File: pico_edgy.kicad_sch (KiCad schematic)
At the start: 18 parts, among them J2 001, J3 002, J4 007, J5 100, J6 100, J7 USB_C_Receptacle_USB2.0_16P, U4 USBLC6-2SC6, U5 AMS1117-3.3

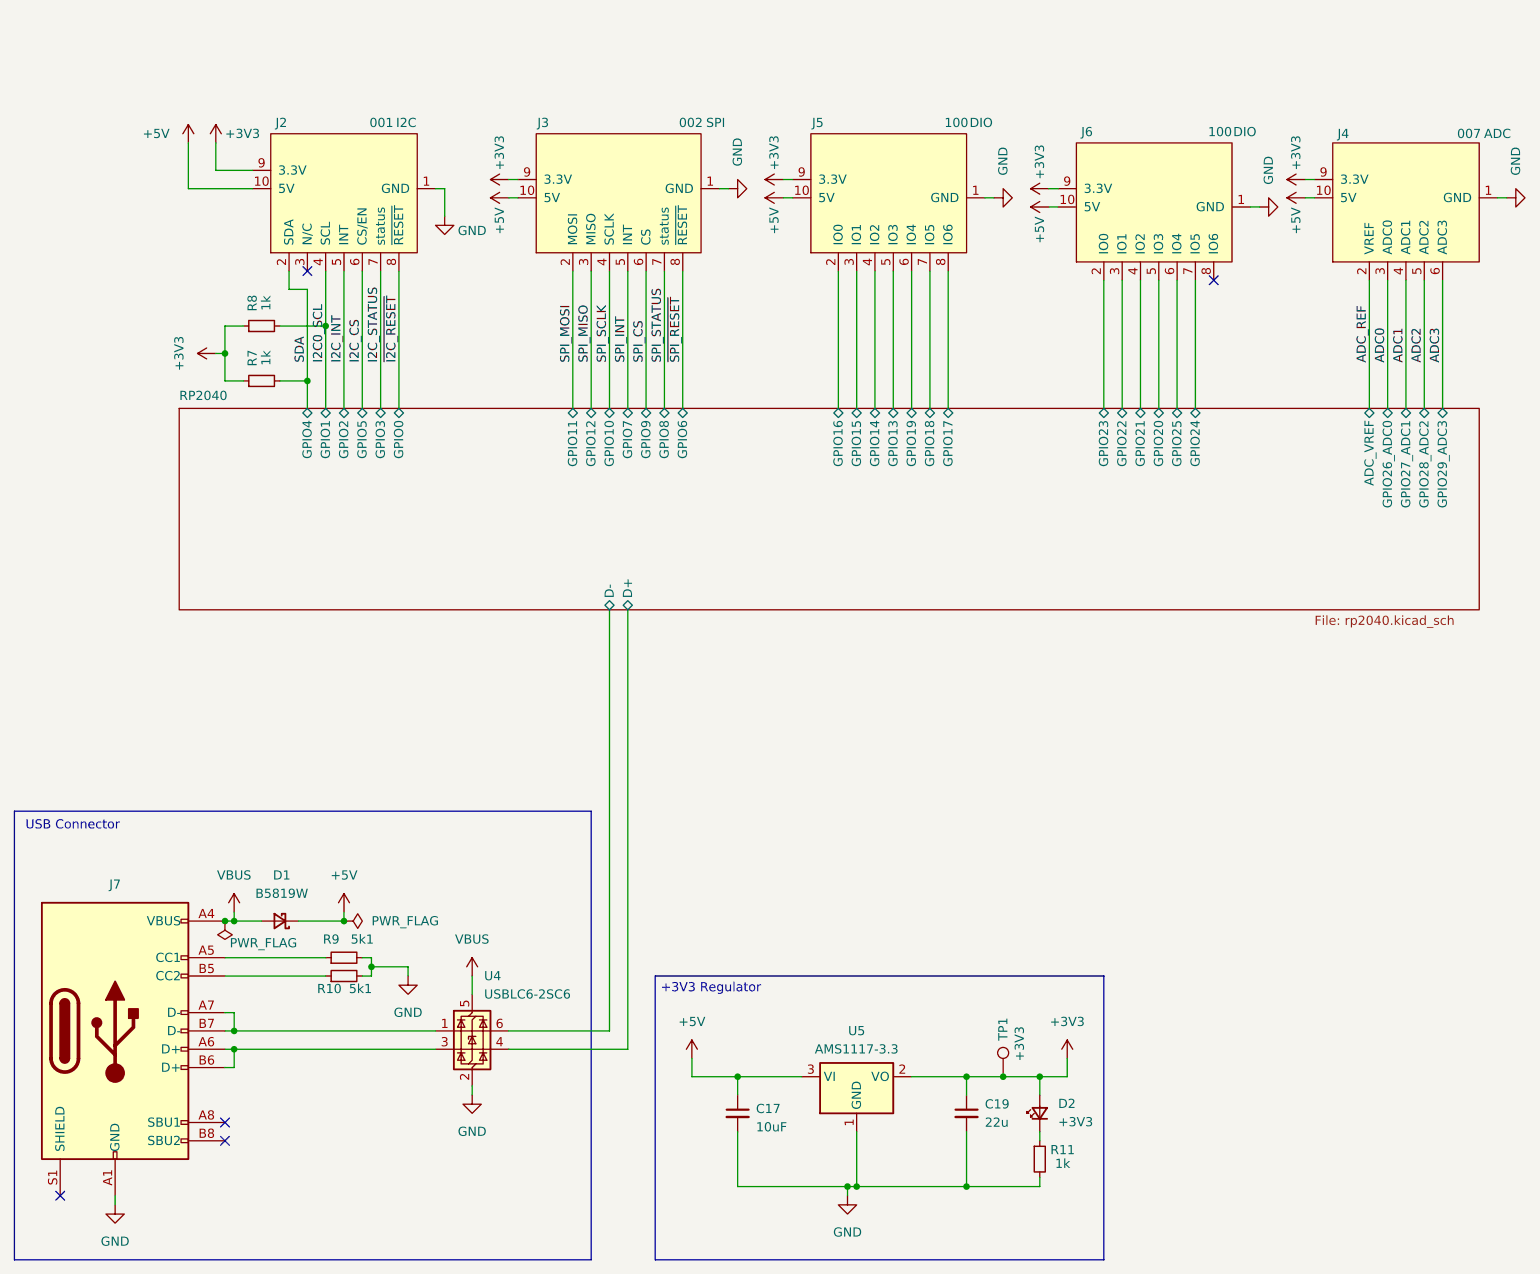
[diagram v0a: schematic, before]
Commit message: layout from scratch, change some components to basic JLCPCB parts
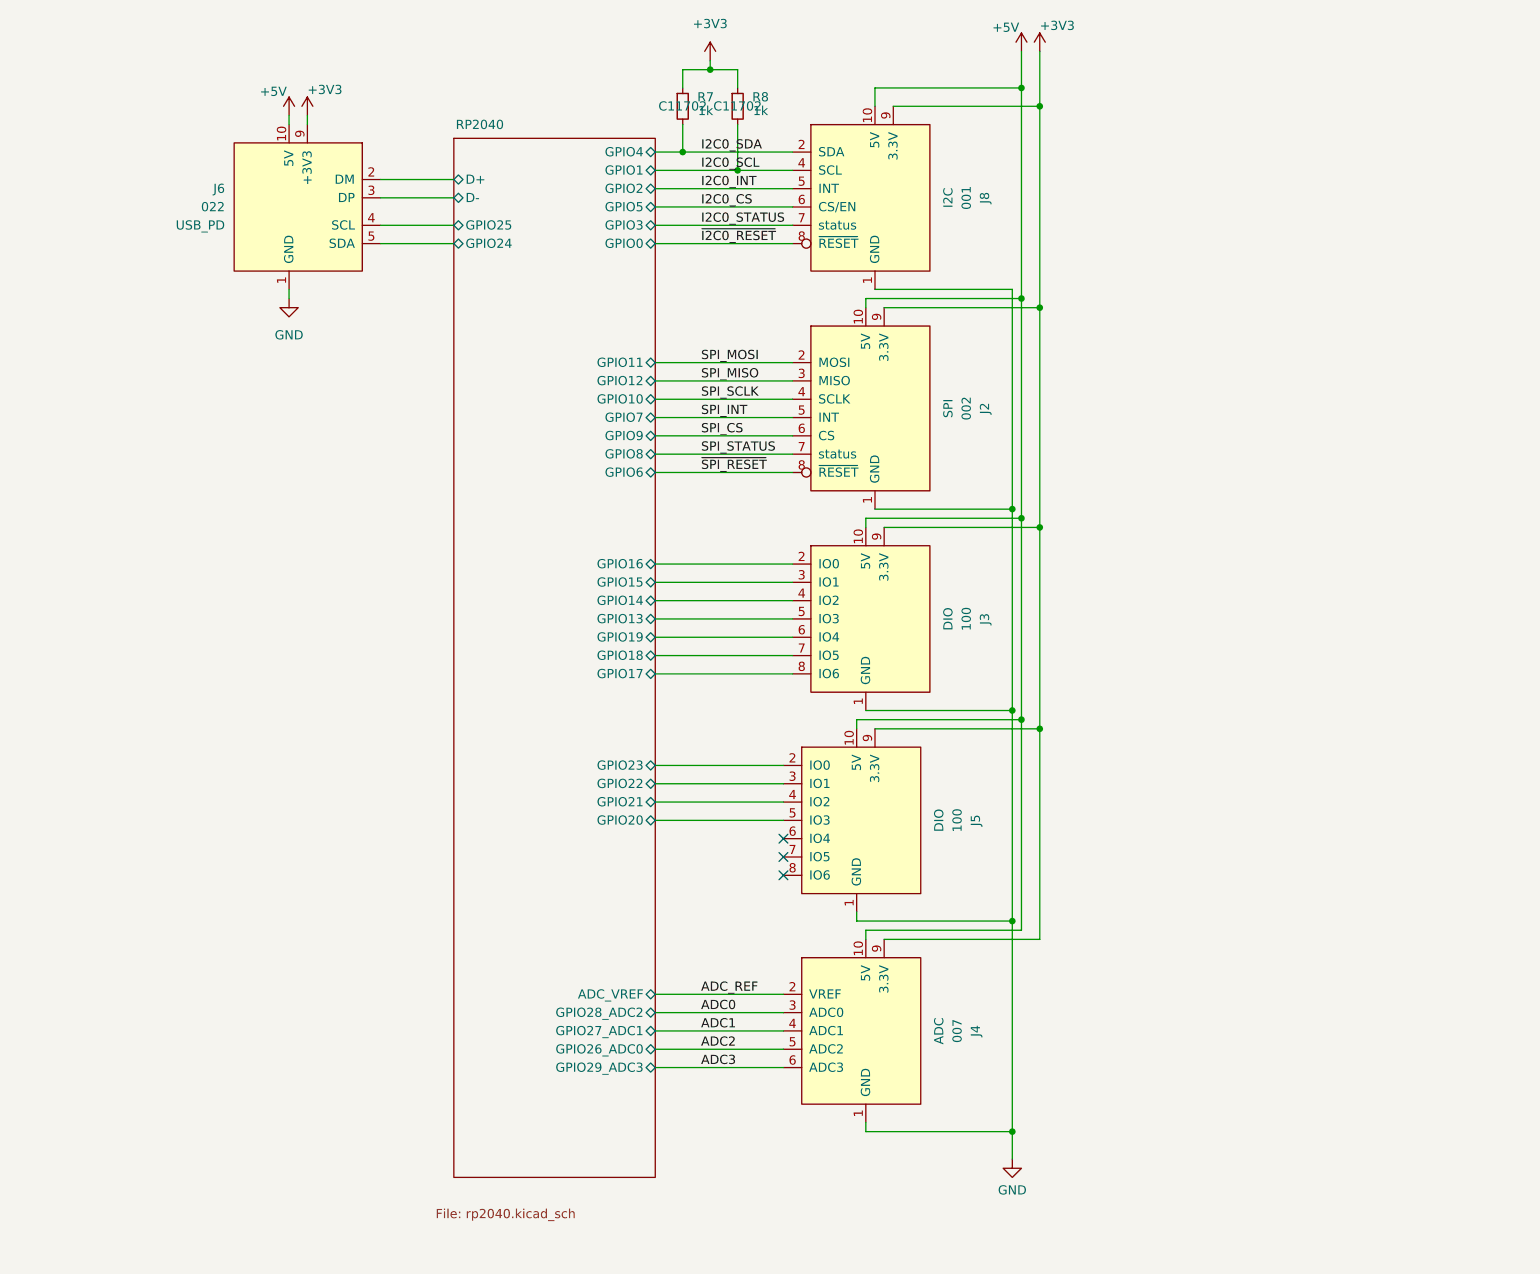
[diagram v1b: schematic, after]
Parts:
- removed C17: 10uF, Capacitor_SMD:C_1210_3225Metric_Pad1.33x2.70mm_HandSolder, symbol Device:C_Small
- removed C19: 22u, Capacitor_SMD:C_1206_3216Metric_Pad1.33x1.80mm_HandSolder, symbol Device:C_Small
- removed D1: B5819W, Diode_SMD:D_SOD-123, symbol Device:D_Schottky_Small
- removed D2: +3V3, LED_SMD:LED_0603_1608Metric_Pad1.05x0.95mm_HandSolder, symbol Device:LED_Small
- removed J2: 001, on_edge:on_edge_2x05_host, symbol put_on_edge:001_I2C
- removed J3: 002, on_edge:on_edge_2x05_host, symbol put_on_edge:002_SPI
- removed J4: 007, on_edge:on_edge_2x05_host, symbol put_on_edge:007_ADC
- removed J5, J6: 100, on_edge:on_edge_2x05_host, symbol put_on_edge:100_digital_IO
- removed J7: USB_C_Receptacle_USB2.0_16P, on_edge:USB_C_Receptacle_Palconn_UTC16-G, symbol Connector:USB_C_Receptacle_USB2.0_16P
- removed R10, R9: 5k1, Resistor_SMD:R_0402_1005Metric_Pad0.72x0.64mm_HandSolder, symbol Device:R_Small
- removed R11: 1k, Resistor_SMD:R_0402_1005Metric, symbol Device:R_Small
- removed TP1: +3V3, TestPoint:TestPoint_THTPad_D1.0mm_Drill0.5mm, symbol Connector:TestPoint
- removed U4: USBLC6-2SC6, Package_TO_SOT_SMD:SOT-23-6, symbol Power_Protection:USBLC6-2SC6
- removed U5: AMS1117-3.3, Package_TO_SOT_SMD:SOT-223-3_TabPin2, symbol Regulator_Linear:AMS1117-3.3
- added J2: 002, put_on_edge:on_edge_2x05_host, symbol put_on_edge:002_SPI_host
- added J3, J5: 100, put_on_edge:on_edge_2x05_host, symbol put_on_edge:100_digital_IO_host
- added J4: 007, put_on_edge:on_edge_2x05_host, symbol put_on_edge:007_ADC_host
- added J6: 022, put_on_edge:on_edge_2x05_host, symbol put_on_edge:026_USB_PD_host
- added J8: 001, put_on_edge:on_edge_2x05_host, symbol put_on_edge:001_I2C_host
- R7, R8: LCSC Part# (none) -> C11702
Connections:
- net +3V3: now also J2.9 (3.3V), J3.9 (3.3V), J4.9 (3.3V), J5.9 (3.3V), J6.9 (+3V3), J8.9 (3.3V)
- net +5V: now also J2.10 (5V), J3.10 (5V), J4.10 (5V), J5.10 (5V), J6.10 (5V), J8.10 (5V)
- net ADC0: now also J4.3 (ADC0)
- net ADC1: now also J4.4 (ADC1)
- net ADC2: now also J4.5 (ADC2)
- net ADC3: now also J4.6 (ADC3)
- net ADC_REF: now also J4.2 (VREF)
- net GND: now also J2.1 (GND), J3.1 (GND), J4.1 (GND), J5.1 (GND), J6.1 (GND), J8.1 (GND)
- net I2C0_SCL: now also J8.4 (SCL)
- net RP2040/D+: now also J6.2 (DM)
- net RP2040/D-: now also J6.3 (DP)
- net RP2040/GPIO13: now also J3.5 (IO3)
- net RP2040/GPIO14: now also J3.4 (IO2)
- net RP2040/GPIO15: now also J3.3 (IO1)
- net RP2040/GPIO16: now also J3.2 (IO0)
- net RP2040/GPIO17: now also J3.8 (IO6)
- net RP2040/GPIO18: now also J3.7 (IO5)
- net RP2040/GPIO19: now also J3.6 (IO4)
- net RP2040/GPIO20: now also J5.5 (IO3)
- net RP2040/GPIO21: now also J5.4 (IO2)
- net RP2040/GPIO22: now also J5.3 (IO1)
- net RP2040/GPIO23: now also J5.2 (IO0)
- net RP2040/GPIO24: now also J6.5 (SDA)
- net RP2040/GPIO25: now also J6.4 (SCL)
- net SPI_CS: now also J2.6 (CS)
- net SPI_INT: now also J2.5 (INT)
- net SPI_MISO: now also J2.3 (MISO)
- net SPI_MOSI: now also J2.2 (MOSI)
- net SPI_SCLK: now also J2.4 (SCLK)
- net SPI_STATUS: now also J2.7 (status)
- net ~{SPI_RESET}: now also J2.8 (~{RESET})
- net SDA renamed I2C0_SDA
- net I2C0_SDA: now also J8.2 (SDA)
- new net I2C0_CS: J8.6 (CS/EN)
- new net I2C0_INT: J8.5 (INT)
- new net I2C0_STATUS: J8.7 (status)
- new net ~{I2C0_RESET}: J8.8 (~{RESET})
- no-connect marks 5 -> 3
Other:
- note removed: "+3V3 Regulator"
- note removed: "USB Connector"
- moved on the sheet: R7, R8
